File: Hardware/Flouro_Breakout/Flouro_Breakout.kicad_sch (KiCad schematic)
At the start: 7 parts, among them J1 Conn_02x20_Odd_Even_MountingP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, J2 Conn_02x20_Odd_Even_MountingP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

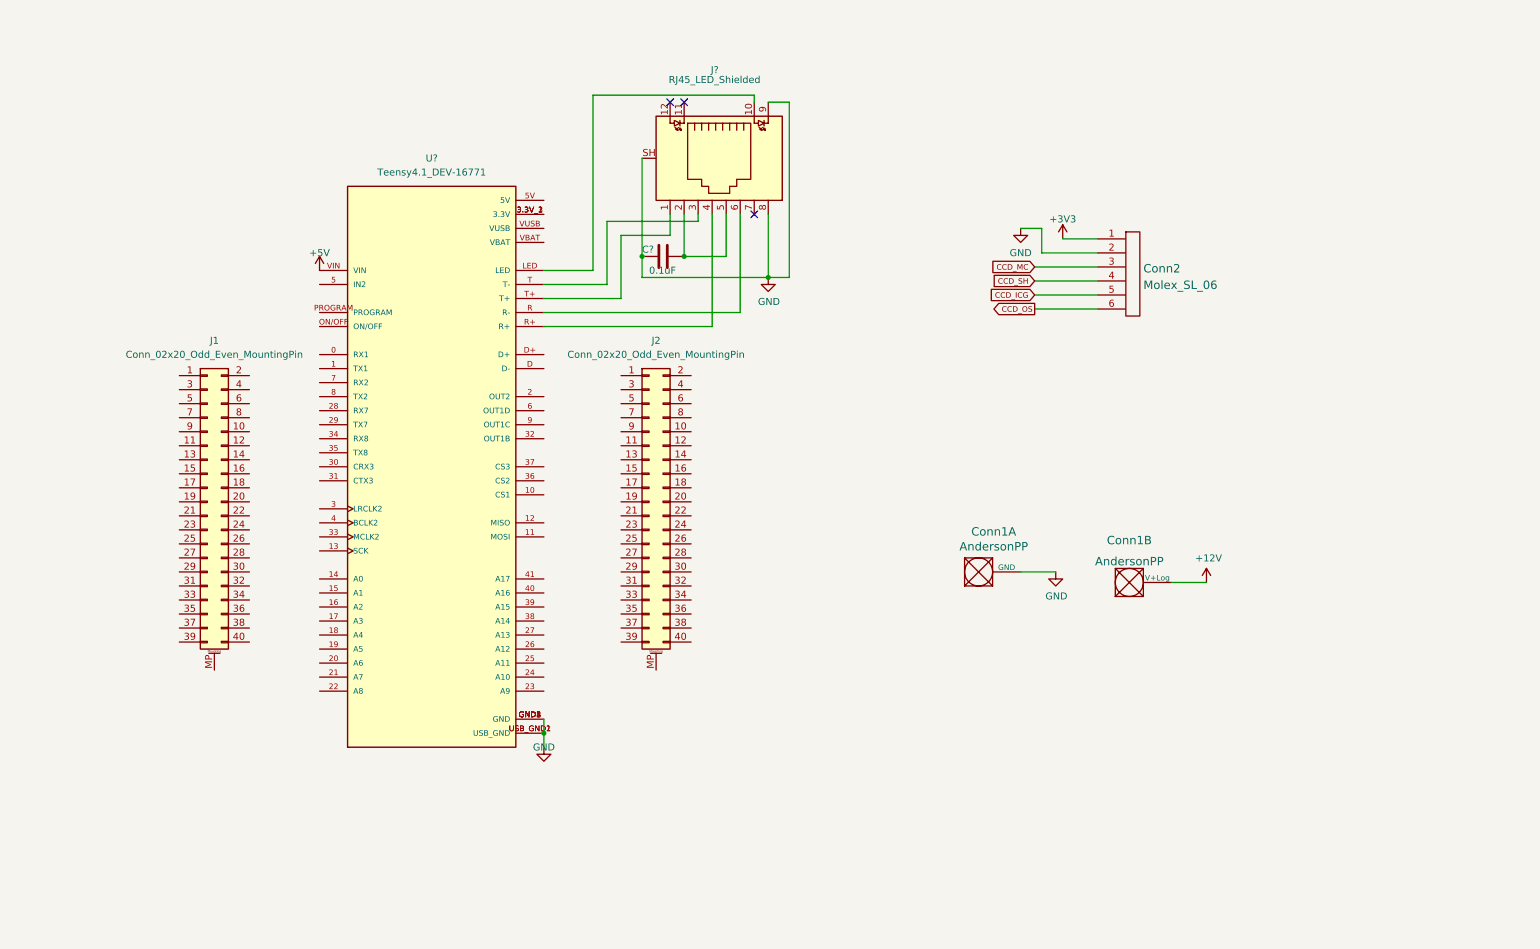
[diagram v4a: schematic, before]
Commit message: Finalizing schematic component placement
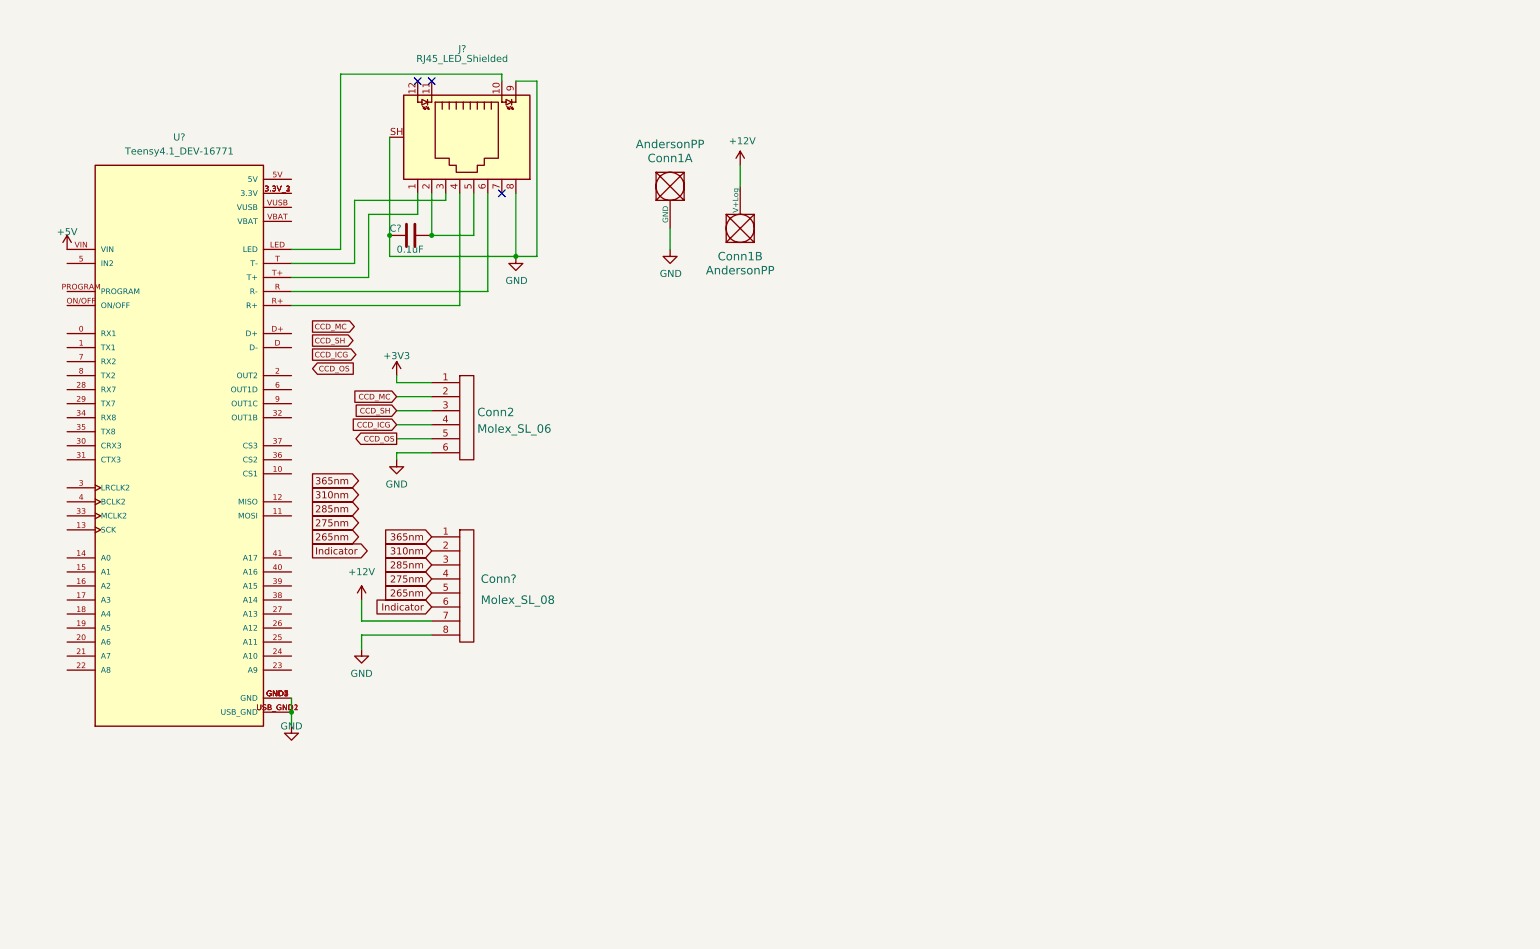
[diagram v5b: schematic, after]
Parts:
- removed J1, J2: Conn_02x20_Odd_Even_MountingPin, symbol Connector_Generic_MountingPin:Conn_02x20_Odd_Even_MountingPin
- added Conn?: Molex_SL_08, symbol MRDT_Connectors:Molex_SL_08
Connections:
- net +12V: now also Conn?.7
- net CCD_ICG: now also Conn2.4; no longer Conn2.5
- net CCD_MC: now also Conn2.2; no longer Conn2.3
- net CCD_OS: now also Conn2.5; no longer Conn2.6
- net CCD_SH: now also Conn2.3; no longer Conn2.4
- net GND: now also Conn2.6, Conn?.8; no longer Conn2.2
- new net 265nm: Conn?.5
- new net 275nm: Conn?.4
- new net 285nm: Conn?.3
- new net 310nm: Conn?.2
- new net 365nm: Conn?.1
- new net Indicator: Conn?.6
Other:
- moved on the sheet: C?, Conn1A, Conn1B, Conn2, J?, U?

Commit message: Added power to Fluoro Board
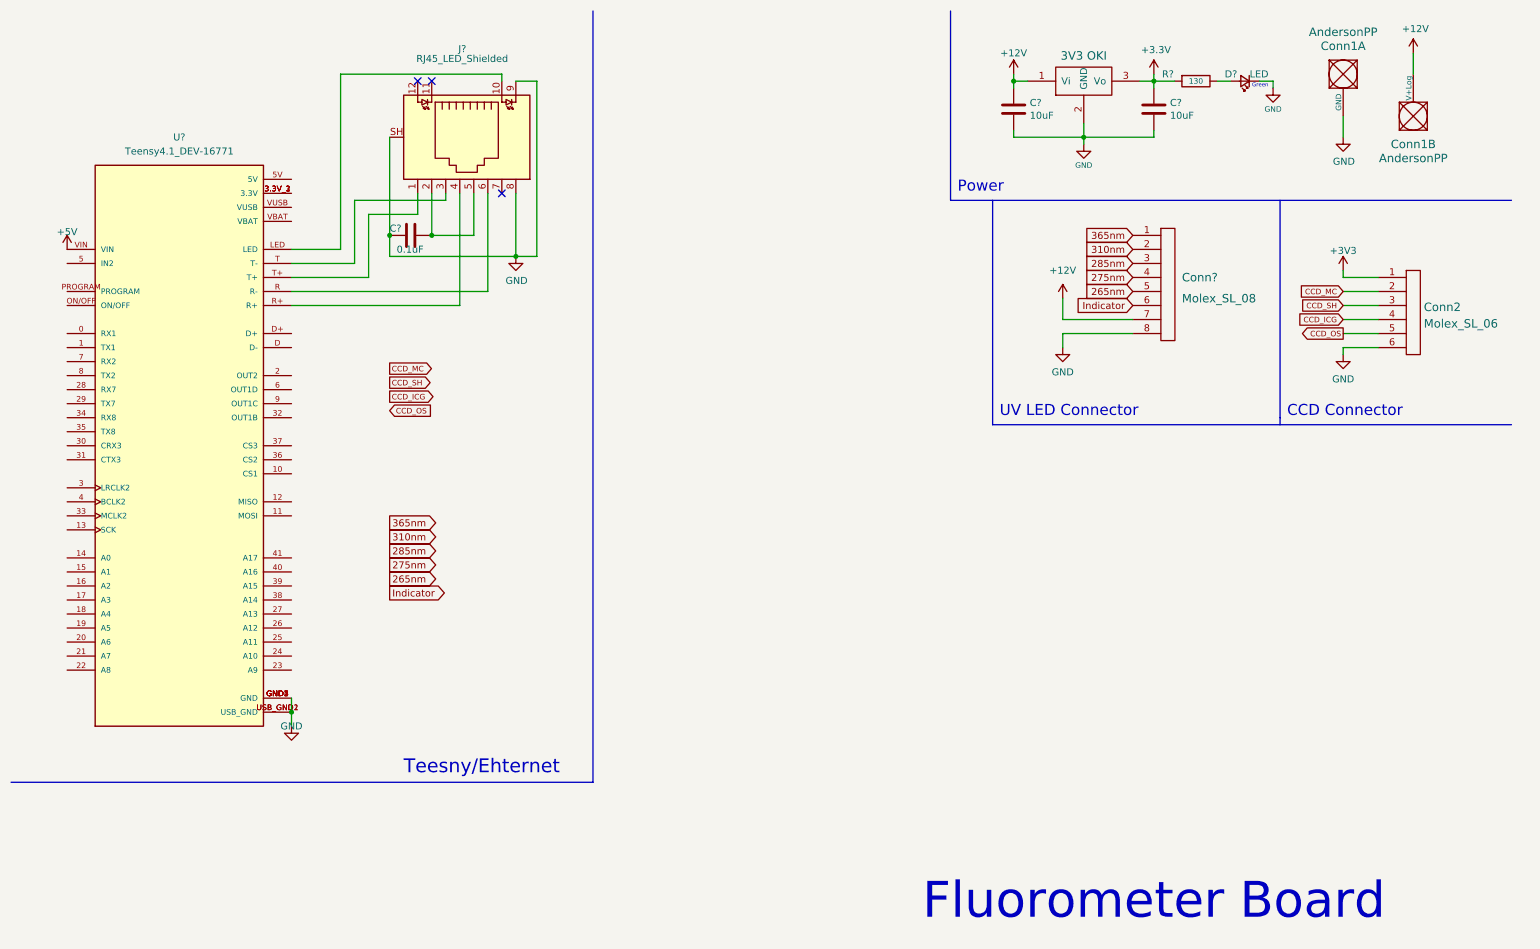
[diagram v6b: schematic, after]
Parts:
- added C? (x2): 10uF, Capacitor_SMD:C_0603_1608Metric_Pad1.08x0.95mm_HandSolder, symbol Device:C
- added D?: LED, LED_SMD:LED_0603_1608Metric_Pad1.05x0.95mm_HandSolder, symbol Device:LED_Small
- added R?: 130, Resistor_SMD:R_0603_1608Metric_Pad0.98x0.95mm_HandSolder, symbol Device:R
- added U?: 3V3 OKI, MRDT_Devices:OKI_Horizontal, symbol MRDT_Devices:OKI
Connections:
- net +12V: now also C?.1, U?.1 (Vi)
- net GND: now also C?.2, C?.2, D?.1 (K), U?.2 (GND)
- new net: D?.2 (A), R?.1
- new net +3.3V: C?.1, R?.2, U?.3 (Vo)
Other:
- note added: "CCD Connector"
- note added: "Fluorometer Board"
- note added: "Green"
- note added: "Power"
- note added: "Teesny/Ehternet"
- note added: "UV LED Connector"
- moved on the sheet: Conn1A, Conn1B, Conn2, Conn?
